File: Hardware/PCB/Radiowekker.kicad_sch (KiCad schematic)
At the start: 0 parts

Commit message: set up general setup project pcb
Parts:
- added LS1, RS1: Speaker, symbol Device:Speaker
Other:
- added sheet FM_reciever (FM_reciever.kicad_sch)
- added sheet Power management (power.kicad_sch)
- added sheet UI Pannel (UI_pannel.kicad_sch)
- added sheet audio controller (audio_controller.kicad_sch)
- added sheet motherboard (motherboard.kicad_sch)
- added sheet screen (screen.kicad_sch)

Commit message: starting schematics uploaded
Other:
- sheet motherboard renamed control board
- sheet screen renamed screen controller
- added sheet Battery management (battery_manager.kicad_sch)
- added sheet USB C (USB_C.kicad_sch)
- moved on the sheet: LS1, RS1
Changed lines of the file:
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@@
 	(symbol
 		(lib_id "Device:Speaker")
-		(at 72.39 57.15 0)
+		(at 133.35 67.31 0)
 		(unit 1)
 		(exclude_from_sim no)
@@
 		(fields_autoplaced yes)
 		(property "Reference" "LS1"
-			(at 77.47 57.1499 0)
+			(at 138.43 67.3099 0)
 			(effects
 				(font
@@
 		)
 		(property "Value" "Speaker"
-			(at 77.47 59.6899 0)
+			(at 138.43 69.8499 0)
 			(effects
 				(font
@@
 		)
 		(property "Footprint" ""
-			(at 72.39 62.23 0)
+			(at 133.35 72.39 0)
 			(effects
 				(font
@@
 		)
 		(property "Datasheet" "~"
-			(at 72.136 58.42 0)
+			(at 133.096 68.58 0)
 			(effects
 				(font
@@
 		)
 		(property "Description" "Speaker"
-			(at 72.39 57.15 0)
+			(at 133.35 67.31 0)
 			(effects
 				(font
@@
 	(symbol
 		(lib_id "Device:Speaker")
-		(at 72.39 71.12 0)
+		(at 133.35 81.28 0)
 		(unit 1)
 		(exclude_from_sim no)
@@
 		(fields_autoplaced yes)
 		(property "Reference" "RS1"
-			(at 77.47 71.1199 0)
+			(at 138.43 81.2799 0)
 			(effects
 				(font
@@
 		)
 		(property "Value" "Speaker"
-			(at 77.47 73.6599 0)
+			(at 138.43 83.8199 0)
 			(effects
 				(font
@@
 		)
 		(property "Footprint" ""
-			(at 72.39 76.2 0)
+			(at 133.35 86.36 0)
 			(effects
 				(font
@@
 		)
 		(property "Datasheet" "~"
-			(at 72.136 72.39 0)
+			(at 133.096 82.55 0)
 			(effects
 				(font
@@
 		)
 		(property "Description" "Speaker"
-			(at 72.39 71.12 0)
+			(at 133.35 81.28 0)
 			(effects
 				(font
@@
 	)
 	(sheet
-		(at 19.05 83.82)
+		(at 81.28 95.25)
 		(size 54.61 39.37)
 		(exclude_from_sim no)
@@
 			(color 0 0 0 0.0000)
 		)
-		(property "Sheetname" "motherboard"
-			(at 19.05 83.1084 0)
+		(property "Sheetname" "control board"
+			(at 81.28 94.5384 0)
 			(effects
 				(font
@@
 		)
 		(property "Sheetfile" "motherboard.kicad_sch"
-			(at 19.05 123.7746 0)
+			(at 81.28 135.2046 0)
 			(effects
 				(font
@@
 	)
 	(sheet
-		(at 19.05 19.05)
+		(at 80.01 29.21)
 		(size 38.1 25.4)
 		(exclude_from_sim no)
@@
 		)
 		(property "Sheetname" "FM_reciever"
-			(at 19.05 18.3384 0)
+			(at 80.01 28.4984 0)
 			(effects
 				(font
@@
 		)
 		(property "Sheetfile" "FM_reciever.kicad_sch"
-			(at 19.05 45.0346 0)
+			(at 80.01 55.1946 0)
 			(effects
 				(font
@@
 	)
 	(sheet
-		(at 86.36 43.18)
+		(at 146.05 99.06)
 		(size 55.88 34.29)
 		(exclude_from_sim no)
@@
 		)
 		(property "Sheetname" "UI Pannel"
-			(at 86.36 42.4684 0)
+			(at 146.05 98.3484 0)
 			(effects
 				(font
@@
 		)
 		(property "Sheetfile" "UI_pannel.kicad_sch"
-			(at 86.36 78.0546 0)
+			(at 146.05 133.9346 0)
 			(effects
 				(font
@@
 	)
 	(sheet
-		(at 86.36 86.36)
+		(at 80.01 143.51)
 		(size 55.88 36.83)
 		(exclude_from_sim no)
@@
 			(color 0 0 0 0.0000)
 		)
-		(property "Sheetname" "screen"
-			(at 86.36 85.6484 0)
+		(property "Sheetname" "screen controller"
+			(at 80.01 142.7984 0)
 			(effects
 				(font
@@
 		)
 		(property "Sheetfile" "screen.kicad_sch"
-			(at 86.36 123.7746 0)
+			(at 80.01 180.9246 0)
 			(effects
 				(font
@@
 	)
 	(sheet
-		(at 19.05 52.07)
+		(at 231.14 106.68)
+		(size 40.64 44.45)
+		(exclude_from_sim no)
+		(in_bom yes)
+		(on_board yes)
+		(dnp no)
+		(fields_autoplaced yes)
+		(stroke
+			(width 0.1524)
+			(type solid)
+		)
+		(fill
+			(color 0 0 0 0.0000)
+		)
+		(property "Sheetname" "Battery management"
+			(at 231.14 105.9684 0)
+			(effects
+				(font
+					(size 1.27 1.27)
+				)
+				(justify left bottom)
+			)
+		)
+		(property "Sheetfile" "battery_manager.kicad_sch"
+			(at 231.14 151.7146 0)
+			(effects
+				(font
+					(size 1.27 1.27)
+				)
+				(justify left top)
+			)
+		)
+		(instances
+			(project "Radiowekker"
+				(path "/d1c96533-fea5-409f-9018-c843faf96bf8"
+					(page "8")
+				)
+			)
+		)
+	)
+	(sheet
+		(at 80.01 62.23)
 		(size 41.91 25.4)
 		(exclude_from_sim no)
@@
 		)
 		(property "Sheetname" "audio controller"
-			(at 19.05 51.3584 0)
+			(at 80.01 61.5184 0)
 			(effects
 				(font
@@
 		)
 		(property "Sheetfile" "audio_controller.kicad_sch"
-			(at 19.05 78.0546 0)
+			(at 80.01 88.2146 0)
 			(effects
 				(font
@@
 	)
 	(sheet
-		(at 17.78 144.78)
+		(at 17.78 95.25)
+		(size 44.45 39.37)
+		(exclude_from_sim no)
+		(in_bom yes)
+		(on_board yes)
+		(dnp no)
+		(fields_autoplaced yes)
+		(stroke
+			(width 0.1524)
+			(type solid)
+		)
+		(fill
+			(color 0 0 0 0.0000)
+		)
+		(property "Sheetname" "USB C"
+			(at 17.78 94.5384 0)
+			(effects
+				(font
+					(size 1.27 1.27)
+				)
+				(justify left bottom)
+			)
+		)
+		(property "Sheetfile" "USB_C.kicad_sch"
+			(at 17.78 135.2046 0)
+			(effects
+				(font
+					(size 1.27 1.27)
+				)
+				(justify left top)
+			)
+		)
+		(instances
+			(project "Radiowekker"
+				(path "/d1c96533-fea5-409f-9018-c843faf96bf8"
+					(page "9")
+				)
+			)
+		)
+	)
+	(sheet
+		(at 231.14 55.88)
 		(size 46.99 44.45)
 		(exclude_from_sim no)
@@
 		(on_board yes)
 		(dnp no)
-		(fields_autoplaced yes)
 		(stroke
 			(width 0.1524)
@@
 		)
 		(property "Sheetname" "Power management"
-			(at 17.78 144.0684 0)
+			(at 231.14 55.1684 0)
 			(effects
 				(font
@@
 		)
 		(property "Sheetfile" "power.kicad_sch"
-			(at 17.78 189.8146 0)
-			(effects
-				(font
+			(at 231.14 100.9146 0)
+			(effects
+				(font

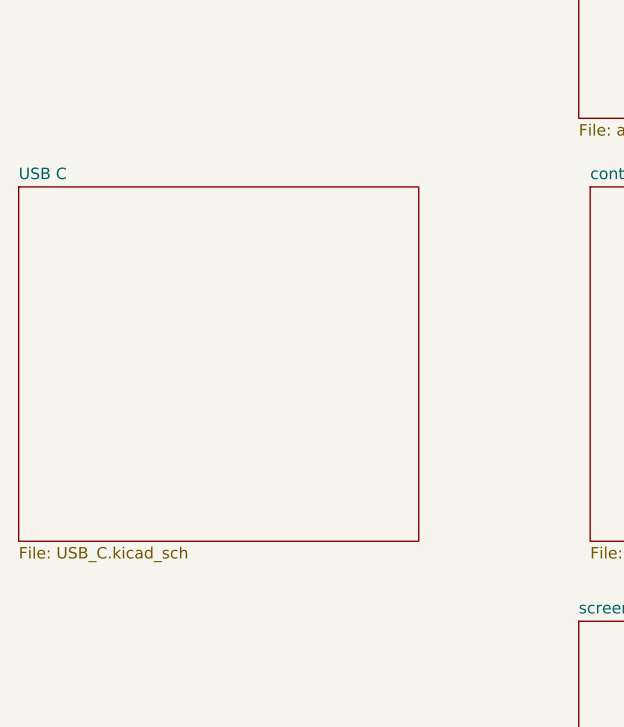
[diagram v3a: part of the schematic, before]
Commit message: adding power management
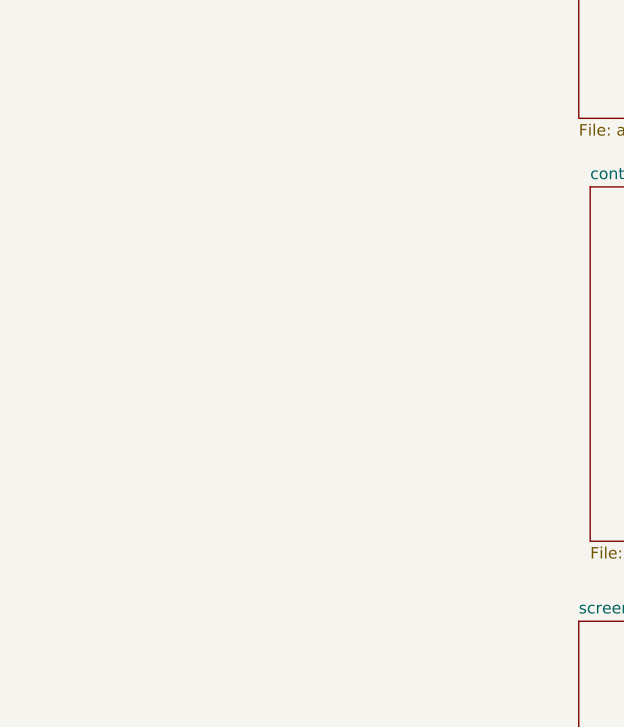
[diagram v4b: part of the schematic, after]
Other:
- removed sheet USB C
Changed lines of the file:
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@@
-	)
-	(sheet
-		(at 17.78 95.25)
-		(size 44.45 39.37)
-		(exclude_from_sim no)
-		(in_bom yes)
-		(on_board yes)
-		(dnp no)
-		(fields_autoplaced yes)
-		(stroke
-			(width 0.1524)
-			(type solid)
-		)
-		(fill
-			(color 0 0 0 0)
-		)
-		(property "Sheetname" "USB C"
-			(at 17.78 94.5384 0)
-			(show_name no)
-			(do_not_autoplace no)
-			(effects
-				(font
-					(size 1.27 1.27)
-				)
-				(justify left bottom)
-			)
-		)
-		(property "Sheetfile" "USB_C.kicad_sch"
-			(at 17.78 135.2046 0)
-			(show_name no)
-			(do_not_autoplace no)
-			(effects
-				(font
-					(size 1.27 1.27)
-				)
-				(justify left top)
-			)
-		)
-		(instances
-			(project "Radiowekker"
-				(path "/d1c96533-fea5-409f-9018-c843faf96bf8"
-					(page "9")
-				)
-			)
-		)
 	)
 	(sheet

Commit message: added UI
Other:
- sheet UI Pannel renamed UI
- removed sheet screen controller
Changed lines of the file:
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@@
 	)
 	(sheet
-		(at 146.05 99.06)
-		(size 55.88 34.29)
+		(at 138.43 95.25)
+		(size 55.88 39.37)
 		(exclude_from_sim no)
 		(in_bom yes)
@@
 			(color 0 0 0 0)
 		)
-		(property "Sheetname" "UI Pannel"
-			(at 146.05 98.3484 0)
+		(property "Sheetname" "UI"
+			(at 138.43 94.5384 0)
 			(show_name no)
 			(do_not_autoplace no)
@@
 		)
 		(property "Sheetfile" "UI_pannel.kicad_sch"
-			(at 146.05 133.9346 0)
+			(at 138.43 135.2046 0)
 			(show_name no)
 			(do_not_autoplace no)
@@
 				)
 			)
-		)
-	)
-	(sheet
-		(at 80.01 143.51)
-		(size 55.88 36.83)
-		(exclude_from_sim no)
-		(in_bom yes)
-		(on_board yes)
-		(dnp no)
-		(fields_autoplaced yes)
-		(stroke
-			(width 0.1524)
-			(type solid)
-		)
-		(fill
-			(color 0 0 0 0)
-		)
-		(property "Sheetname" "screen controller"
-			(at 80.01 142.7984 0)
-			(show_name no)
-			(do_not_autoplace no)
-			(effects
-				(font
-					(size 1.27 1.27)
-				)
-				(justify left bottom)
-			)
-		)
-		(property "Sheetfile" "screen.kicad_sch"
-			(at 80.01 180.9246 0)
-			(show_name no)
-			(do_not_autoplace no)
-			(effects
-				(font
-					(size 1.27 1.27)
-				)
-				(justify left top)
-			)
-		)
-		(instances
-			(project "Radiowekker"
-				(path "/d1c96533-fea5-409f-9018-c843faf96bf8"
-					(page "7")
-				)
-			)

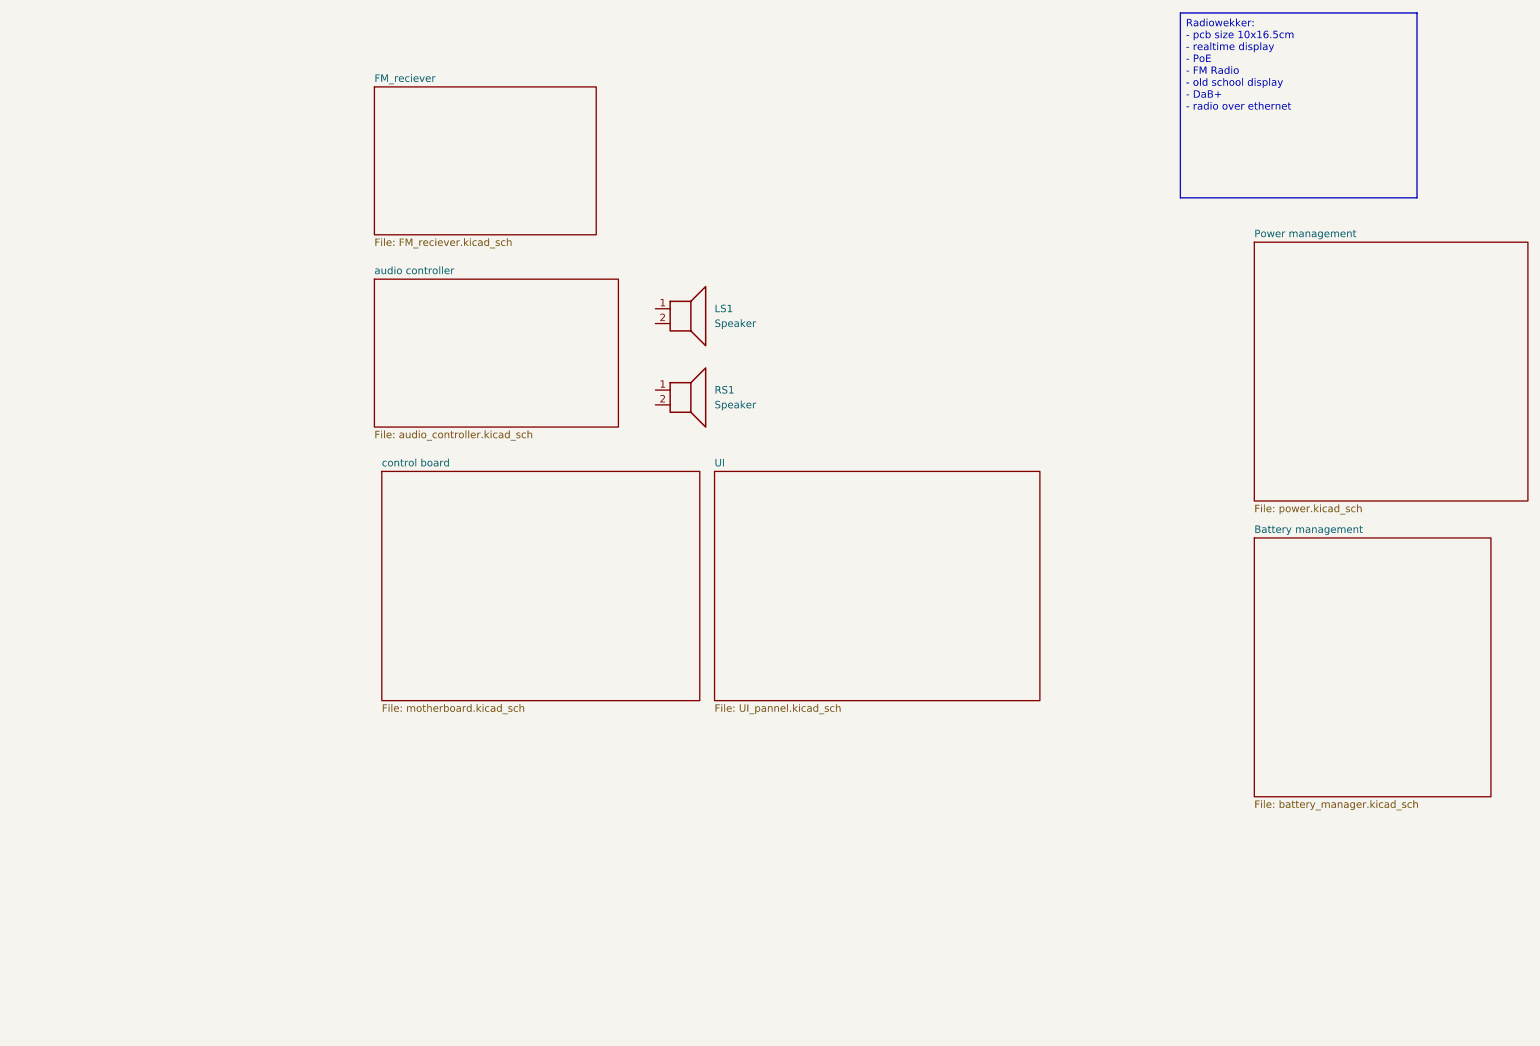
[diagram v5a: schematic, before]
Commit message: added buttons
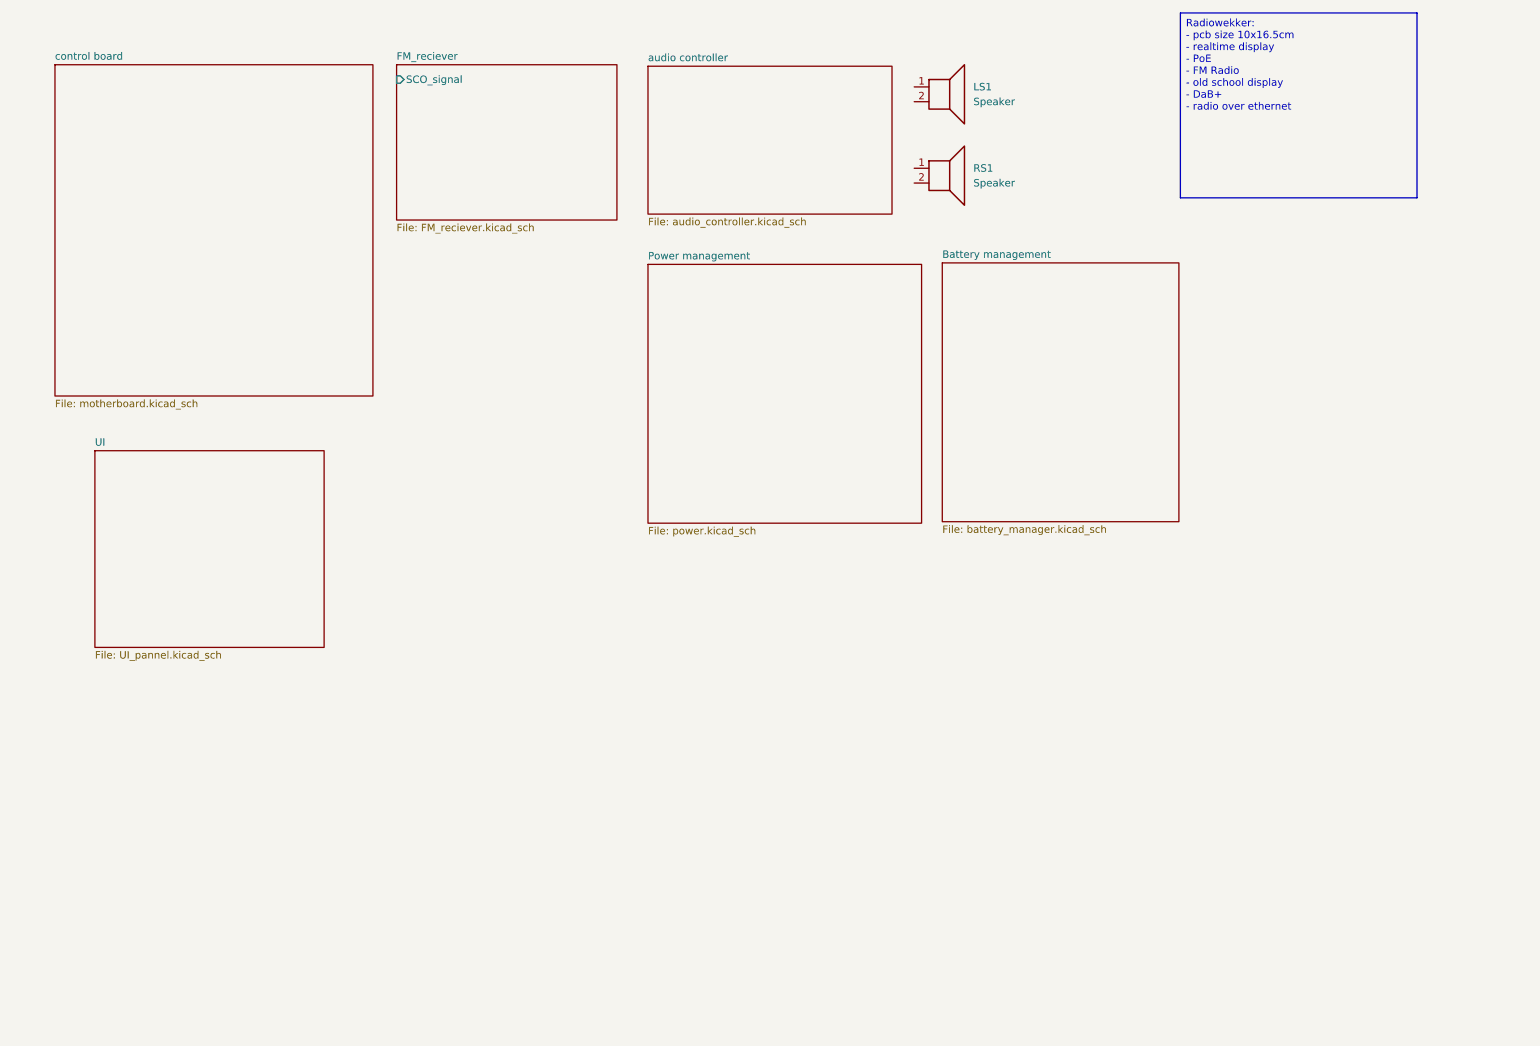
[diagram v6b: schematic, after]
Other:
- sheet FM_reciever ports: added SCO_signal; removed none
- moved on the sheet: LS1, RS1
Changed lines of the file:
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@@
 	(symbol
 		(lib_id "Device:Speaker")
-		(at 133.35 67.31 0)
+		(at 177.8 29.21 0)
 		(unit 1)
 		(body_style 1)
@@
 		(fields_autoplaced yes)
 		(property "Reference" "LS1"
-			(at 138.43 67.3099 0)
+			(at 182.88 29.2099 0)
 			(show_name no)
 			(do_not_autoplace no)
@@
 		)
 		(property "Value" "Speaker"
-			(at 138.43 69.8499 0)
+			(at 182.88 31.7499 0)
 			(show_name no)
 			(do_not_autoplace no)
@@
 		)
 		(property "Footprint" ""
-			(at 133.35 72.39 0)
+			(at 177.8 34.29 0)
 			(hide yes)
 			(show_name no)
@@
 		)
 		(property "Datasheet" ""
-			(at 133.096 68.58 0)
+			(at 177.546 30.48 0)
 			(hide yes)
 			(show_name no)
@@
 		)
 		(property "Description" "Speaker"
-			(at 133.35 67.31 0)
+			(at 177.8 29.21 0)
 			(hide yes)
 			(show_name no)
@@
 	(symbol
 		(lib_id "Device:Speaker")
-		(at 133.35 81.28 0)
+		(at 177.8 43.18 0)
 		(unit 1)
 		(body_style 1)
@@
 		(fields_autoplaced yes)
 		(property "Reference" "RS1"
-			(at 138.43 81.2799 0)
+			(at 182.88 43.1799 0)
 			(show_name no)
 			(do_not_autoplace no)
@@
 		)
 		(property "Value" "Speaker"
-			(at 138.43 83.8199 0)
+			(at 182.88 45.7199 0)
 			(show_name no)
 			(do_not_autoplace no)
@@
 		)
 		(property "Footprint" ""
-			(at 133.35 86.36 0)
+			(at 177.8 48.26 0)
 			(hide yes)
 			(show_name no)
@@
 		)
 		(property "Datasheet" ""
-			(at 133.096 82.55 0)
+			(at 177.546 44.45 0)
 			(hide yes)
 			(show_name no)
@@
 		)
 		(property "Description" "Speaker"
-			(at 133.35 81.28 0)
+			(at 177.8 43.18 0)
 			(hide yes)
 			(show_name no)
@@
 	)
 	(sheet
-		(at 81.28 95.25)
-		(size 54.61 39.37)
+		(at 25.146 25.4)
+		(size 54.61 56.896)
 		(exclude_from_sim no)
 		(in_bom yes)
@@
 		)
 		(property "Sheetname" "control board"
-			(at 81.28 94.5384 0)
+			(at 25.146 24.6884 0)
 			(show_name no)
 			(do_not_autoplace no)
@@
 		)
 		(property "Sheetfile" "motherboard.kicad_sch"
-			(at 81.28 135.2046 0)
+			(at 25.146 82.8806 0)
 			(show_name no)
 			(do_not_autoplace no)
@@
 	)
 	(sheet
-		(at 80.01 29.21)
-		(size 38.1 25.4)
+		(at 83.82 25.4)
+		(size 37.846 26.67)
 		(exclude_from_sim no)
 		(in_bom yes)
@@
 		)
 		(property "Sheetname" "FM_reciever"
-			(at 80.01 28.4984 0)
+			(at 83.82 24.6884 0)
 			(show_name no)
 			(do_not_autoplace no)
@@
 		)
 		(property "Sheetfile" "FM_reciever.kicad_sch"
-			(at 80.01 55.1946 0)
+			(at 83.82 52.6546 0)
 			(show_name no)
 			(do_not_autoplace no)
@@
 			)
 		)
+		(pin "SCO_signal" input
+			(at 83.82 27.94 180)
+			(effects
+				(font
+					(size 1.27 1.27)
+				)
+				(justify left)
+			)
+		)
 		(instances
 			(project "Radiowekker"
@@
 	)
 	(sheet
-		(at 138.43 95.25)
-		(size 55.88 39.37)
+		(at 32.004 91.694)
+		(size 39.37 33.782)
 		(exclude_from_sim no)
 		(in_bom yes)
@@
 		)
 		(property "Sheetname" "UI"
-			(at 138.43 94.5384 0)
+			(at 32.004 90.9824 0)
 			(show_name no)
 			(do_not_autoplace no)
@@
 		)
 		(property "Sheetfile" "UI_pannel.kicad_sch"
-			(at 138.43 135.2046 0)
+			(at 32.004 126.0606 0)
 			(show_name no)
 			(do_not_autoplace no)
@@
 	)
 	(sheet
-		(at 231.14 106.68)
+		(at 177.546 59.436)
 		(size 40.64 44.45)
 		(exclude_from_sim no)
@@
 		)
 		(property "Sheetname" "Battery management"
-			(at 231.14 105.9684 0)
+			(at 177.546 58.7244 0)
 			(show_name no)
 			(do_not_autoplace no)
@@
 		)
 		(property "Sheetfile" "battery_manager.kicad_sch"
-			(at 231.14 151.7146 0)
+			(at 177.546 104.4706 0)
 			(show_name no)
 			(do_not_autoplace no)
@@
 	)
 	(sheet
-		(at 80.01 62.23)
+		(at 127 25.654)
 		(size 41.91 25.4)
 		(exclude_from_sim no)
@@
 		)
 		(property "Sheetname" "audio controller"
-			(at 80.01 61.5184 0)
+			(at 127 24.9424 0)
 			(show_name no)
 			(do_not_autoplace no)
@@
 		)
 		(property "Sheetfile" "audio_controller.kicad_sch"
-			(at 80.01 88.2146 0)
+			(at 127 51.6386 0)
 			(show_name no)
 			(do_not_autoplace no)
@@
 	)
 	(sheet
-		(at 231.14 55.88)
+		(at 127 59.69)
 		(size 46.99 44.45)
 		(exclude_from_sim no)
@@
 		)
 		(property "Sheetname" "Power management"
-			(at 231.14 55.1684 0)
+			(at 127 58.9784 0)
 			(show_name no)
 			(do_not_autoplace no)
@@
 		)
 		(property "Sheetfile" "power.kicad_sch"
-			(at 231.14 100.9146 0)
-			(show_name no)
-			(do_not_autoplace no)
+			(at 127 104.7246 0)
+			(show_name no)
+			(do_not_autoplace no)
